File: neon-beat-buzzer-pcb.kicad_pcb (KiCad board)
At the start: 2 copper layers, 117.5 x 54.5 mm, 57 parts, among them J1 BATT_CON, J2 SWITCH_CON, J3 BUTTON_CON, J4 USB_C_Receptacle_USB2.0_16P, U1 ESP32-C3-MINI-1, U2 BQ24074RGT, U3 TPS22929D, U4 MCP1700x-330xxTT, U5 TPS610997DRV, U6 USBLC6-2SC6

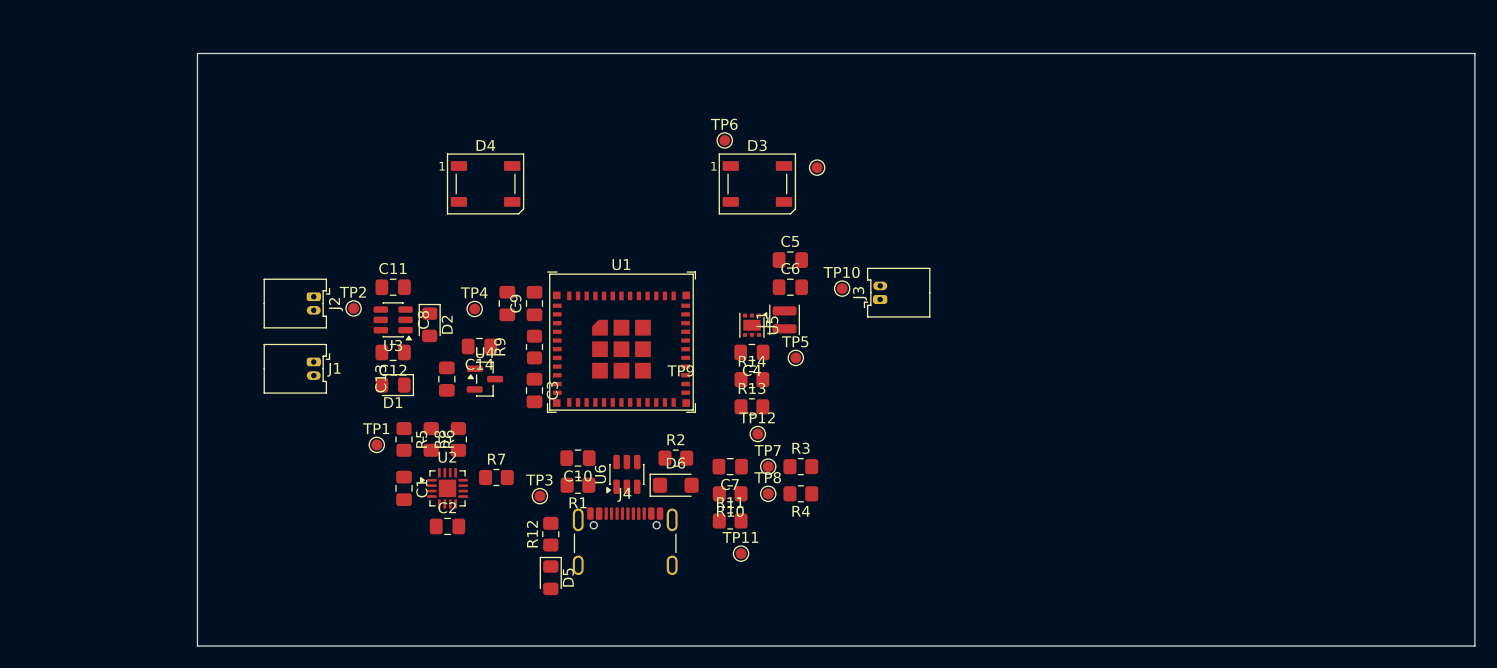
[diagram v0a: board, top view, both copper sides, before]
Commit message: pcb: add layout from Freecad
Signed-off-by: Alexis Lothoré <alexis.lothore@gmail.com>
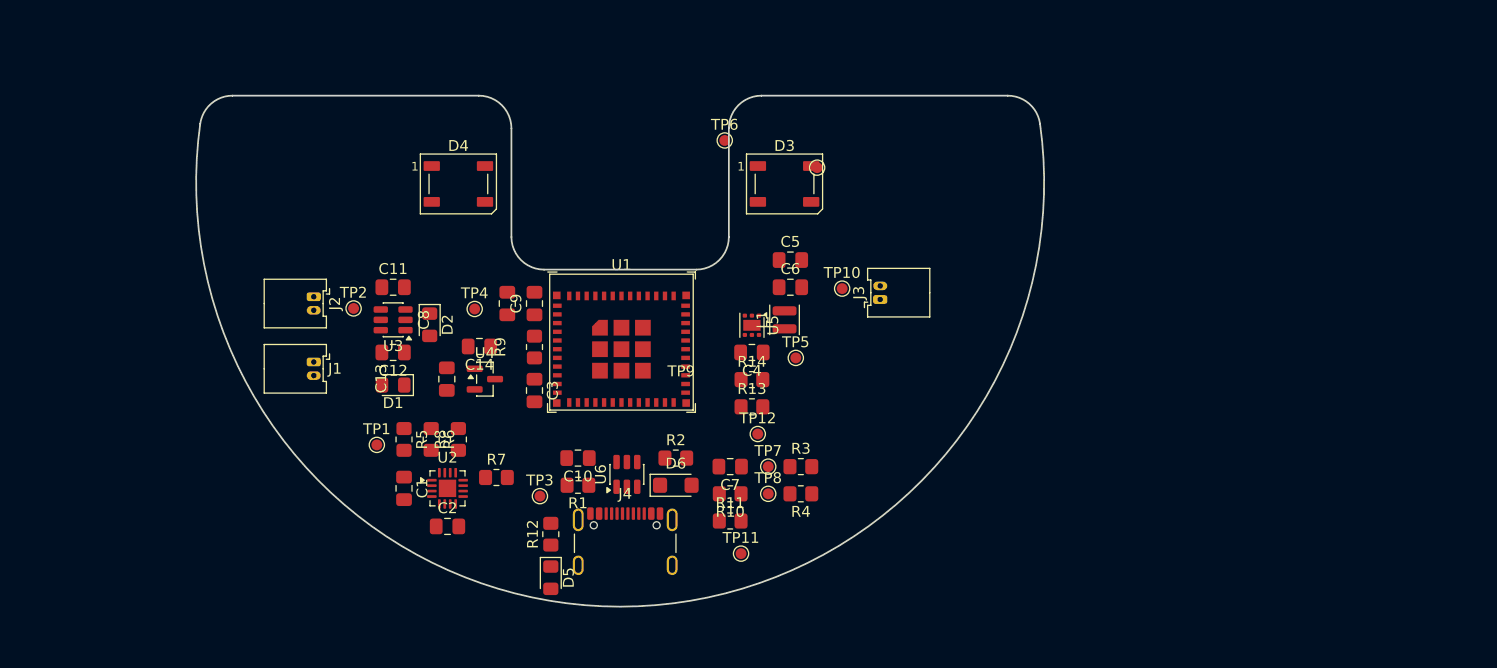
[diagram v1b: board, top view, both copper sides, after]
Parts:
- moved D3 2.50 mm to (165.0, 100.0)
- moved D4 2.50 mm to (135.0, 100.0)
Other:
- board size 117.5 x 54.5 mm -> 78 x 47 mm
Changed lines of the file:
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@@
 	(footprint "LED_SMD:LED_WS2812B_PLCC4_5.0x5.0mm_P3.2mm"
 		(layer "F.Cu")
-		(at 137.5 100)
+		(at 135 100)
 		(descr "5.0mm x 5.0mm Addressable RGB LED NeoPixel, https://cdn-shop.adafruit.com/datasheets/WS2812B.pdf")
 		(tags "LED RGB NeoPixel PLCC-4 5050")
@@
 	(footprint "LED_SMD:LED_WS2812B_PLCC4_5.0x5.0mm_P3.2mm"
 		(layer "F.Cu")
-		(at 162.5 100)
+		(at 165 100)
 		(descr "5.0mm x 5.0mm Addressable RGB LED NeoPixel, https://cdn-shop.adafruit.com/datasheets/WS2812B.pdf")
 		(tags "LED RGB NeoPixel PLCC-4 5050")
@@
 		)
 	)
-	(gr_rect
-		(start 111 88)
-		(end 228.5 142.5)
+	(gr_arc
+		(start 111.256669 94.462013)
+		(mid 112.259091 92.614834)
+		(end 114.227593 91.87868)
 		(stroke
-			(width 0.05)
-			(type default)
+			(width 0.16)
+			(type solid)
+		)
+		(layer "Edge.Cuts")
+	)
+	(gr_line
+		(start 114.227593 91.87868)
+		(end 136.87868 91.87868)
+		(stroke
+			(width 0.16)
+			(type solid)
+		)
+		(layer "Edge.Cuts")
+	)
+	(gr_arc
+		(start 136.87868 91.87868)
+		(mid 139 92.75736)
+		(end 139.87868 94.87868)
+		(stroke
+			(width 0.16)
+			(type solid)
+		)
+		(layer "Edge.Cuts")
+	)
+	(gr_line
+		(start 139.87868 94.87868)
+		(end 139.87868 104.87868)
+		(stroke
+			(width 0.16)
+			(type solid)
+		)
+		(layer "Edge.Cuts")
+	)
+	(gr_arc
+		(start 142.87868 107.87868)
+		(mid 140.75736 107)
+		(end 139.87868 104.87868)
+		(stroke
+			(width 0.16)
+			(type solid)
+		)
+		(layer "Edge.Cuts")
+	)
+	(gr_line
+		(start 142.87868 107.87868)
+		(end 156.87868 107.87868)
+		(stroke
+			(width 0.16)
+			(type solid)
+		)
+		(layer "Edge.Cuts")
+	)
+	(gr_arc
+		(start 159.87868 94.87868)
+		(mid 160.75736 92.75736)
+		(end 162.87868 91.87868)
+		(stroke
+			(width 0.16)
+			(type solid)
+		)
+		(layer "Edge.Cuts")
+	)
+	(gr_arc
+		(start 159.87868 104.87868)
+		(mid 159 107)
+		(end 156.87868 107.87868)
+		(stroke
+			(width 0.16)
+			(type solid)
+		)
+		(layer "Edge.Cuts")
+	)
+	(gr_line
+		(start 159.87868 104.87868)
+		(end 159.87868 94.87868)
+		(stroke
+			(width 0.16)
+			(type solid)
+		)
+		(layer "Edge.Cuts")
+	)
+	(gr_line
+		(start 162.87868 91.87868)
+		(end 185.529767 91.87868)
+		(stroke
+			(width 0.16)
+			(type solid)
+		)
+		(layer "Edge.Cuts")
+	)
+	(gr_arc
+		(start 185.529767 91.87868)
+		(mid 187.498276 92.614829)
+		(end 188.500691 94.462013)
+		(stroke
+			(width 0.16)
+			(type solid)
+		)
+		(layer "Edge.Cuts")
+	)
+	(gr_arc
+		(start 188.500691 94.462013)
+		(mid 149.87868 138.87868)
+		(end 111.256669 94.462013)
+		(stroke
+			(width 0.16)
+			(type solid)
 		)
-		(fill no)
 		(layer "Edge.Cuts")
 	)

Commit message: project: partial routing
Signed-off-by: Alexis Lothoré <alexis.lothore@gmail.com>
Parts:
- added C15: 0.1uF, Capacitor_SMD:C_0805_2012Metric_Pad1.18x1.45mm_HandSolder, F.Cu at (147.0, 89.5)
- added C16: 0.1uF, Capacitor_SMD:C_0805_2012Metric_Pad1.18x1.45mm_HandSolder, F.Cu at (118.0, 89.5)
- added C17: 0.1uF, Capacitor_SMD:C_0805_2012Metric_Pad1.18x1.45mm_HandSolder, F.Cu at (155.0, 115.5)
- added R16: 10k, Resistor_SMD:R_0805_2012Metric_Pad1.20x1.40mm_HandSolder, F.Cu at (164.7, 110.0)
- added U7: XC6210B332MR, Package_TO_SOT_SMD:SOT-23-5, F.Cu at (122.8, 111.8)
- U4: value MCP1700x-330xxTT -> 74AHCT1G125; footprint Package_TO_SOT_SMD:SOT-23 -> Package_TO_SOT_SMD:SOT-23-5
- moved TP5 45.5 mm to (121.5, 106.8)
- moved R4 34.1 mm to (132.5, 125.5), turned to 90 degrees
- moved TP8 33.2 mm to (130.5, 124.5)
- moved R3 32.0 mm to (134.5, 125.5), turned to 90 degrees
- moved TP10 27.5 mm to (143.5, 115.8)
- moved TP7 27.0 mm to (136.5, 124.5)
- moved TP12 26.3 mm to (136.2, 122.2)
- moved R13 23.5 mm to (138.5, 119.8), turned to 180 degrees
- moved J3 23.4 mm to (150.8, 114.5), turned to -90 degrees
- moved R1 22.5 mm to (123.5, 128.5), turned to 90 degrees
- moved U4 20.8 mm to (148.0, 100.0)
- moved R14 20.7 mm to (143.0, 109.8), turned to -90 degrees
- moved TP4 19.5 mm to (117.2, 114.8)
- moved C11 18.5 mm to (110.8, 112.8), turned to 90 degrees
- moved D6 18.0 mm to (137.0, 129.0), turned to 90 degrees
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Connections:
- C4 pad 1: /v_3v3 -> /v_sys
- D3 pad 4: /led -> Net-(D3-DIN)
- L1 pad 1: /v_3v3 -> /v_sys
- R13 pad 2: /v_3v3 -> Net-(U5-EN)
- R14 pad 2: /v_3v3 -> /v_sys
- U4 pad 2: /v_3v3 -> /led
- U4 pad 3: /v_ldo -> GND
- U5 pad 6: /v_3v3 -> /v_sys
- U6 pad 1: Net-(J4-D--PadA7) -> Net-(R4-Pad1)
- U6 pad 3: Net-(J4-D+-PadA6) -> Net-(R3-Pad1)
- U6 pad 4: Net-(R3-Pad1) -> Net-(J4-D+-PadA6)
- U6 pad 6: Net-(R4-Pad1) -> Net-(J4-D--PadA7)
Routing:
- net GND: track 0.00 -> 64.0 mm
- net /v_usb: track 0.00 -> 25.6 mm
- net /v_sys: track 0.00 -> 17.8 mm
- net /v_3v3: track 0.00 -> 15.5 mm
- net Net-(J4-CC1): track 0.00 -> 13.5 mm
- net /v_batt_p: track 0.00 -> 12.5 mm
- net /v_ldo: track 0.00 -> 11.9 mm
- net Net-(J4-CC2): track 0.00 -> 10.4 mm
- net Net-(R3-Pad1): track 0.00 -> 9.20 mm
- net Net-(J4-D--PadA7): track 0.00 -> 6.74 mm
- net /switch: track 0.00 -> 6.62 mm
- net Net-(D1-K): track 0.00 -> 6.47 mm
- net Net-(J4-D+-PadA6): track 0.00 -> 4.92 mm
- net Net-(U1-EN/CHIP_PU): track 0.00 -> 4.13 mm
- net /chg: track 0.00 -> 2.78 mm
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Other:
- board size 78 x 47 mm -> 78 x 55.1 mm

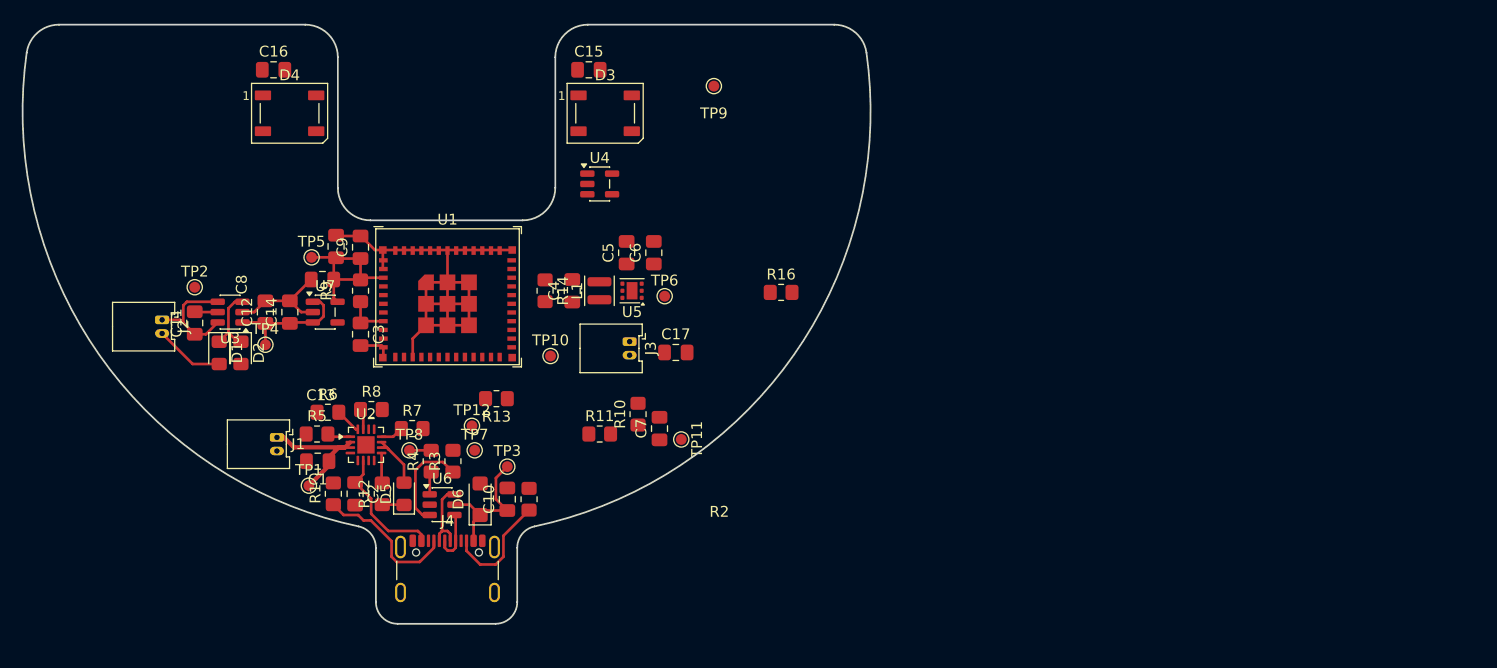
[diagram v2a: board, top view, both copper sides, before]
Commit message: project: add routed board
- Board is now fully routed (and needs some review)
- Tooling holes are added
- Needs to complete BOM

Signed-off-by: Alexis Lothoré <alexis.lothore@gmail.com>
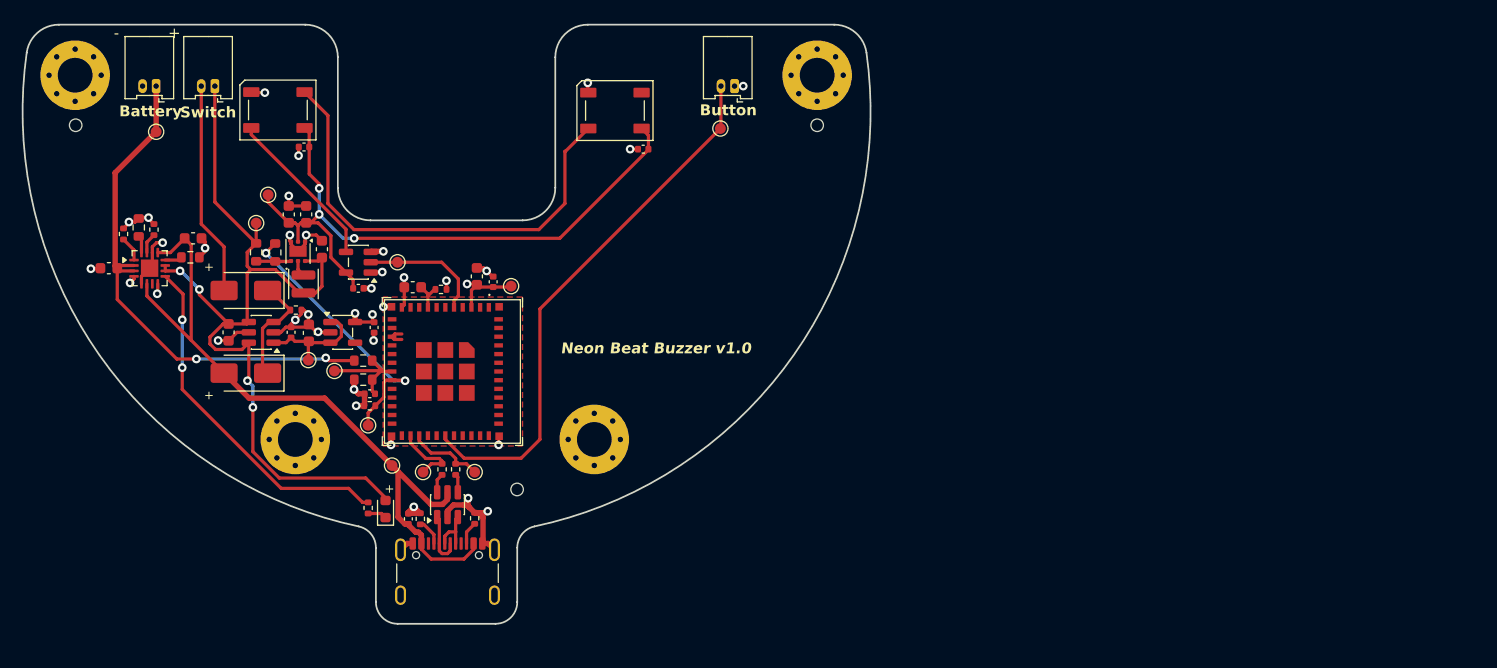
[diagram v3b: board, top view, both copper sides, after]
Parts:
- removed D1, D2: D, Diode_SMD:D_0805_2012Metric_Pad1.15x1.40mm_HandSolder
- removed D6: SMF5V0A, Diode_SMD:D_SMF
- added D7: D_Schottky, Diode_SMD:D_SMA, F.Cu at (115.5, 109.8)
- added D8: D_Schottky, Diode_SMD:D_SMA, F.Cu at (115.5, 117.4)
- added H1: ~, MountingHole:MountingHole_3.2mm_M3_Pad_Via, F.Cu at (99.8, 90.0)
- added H2: ~, MountingHole:MountingHole_3.2mm_M3_Pad_Via, F.Cu at (168.0, 90.0)
- added H3: ~, MountingHole:MountingHole_3.2mm_M3_Pad_Via, F.Cu at (147.5, 123.5)
- added H4: ~, MountingHole:MountingHole_3.2mm_M3_Pad_Via, F.Cu at (120.0, 123.5)
- added R15: 10k, Resistor_SMD:R_0402_1005Metric, F.Cu at (120.0, 111.6)
- added REF**: ToolingHole_1.152mm, MountingHole:ToolingHole_1.152mm, F.Cu at (99.8, 94.6)
- added REF**: ToolingHole_1.152mm, MountingHole:ToolingHole_1.152mm, F.Cu at (140.4, 128.1)
- added REF**: ToolingHole_1.152mm, MountingHole:ToolingHole_1.152mm, F.Cu at (168.0, 94.6)
- C1, C11, C14, C2, C3, C4, C5, C6, C9: footprint Capacitor_SMD:C_0805_2012Metric_Pad1.18x1.45mm_HandSolder -> Capacitor_SMD:C_0603_1608Metric
- C10, C12, C13, C15, C16, C17, C7, C8: footprint Capacitor_SMD:C_0805_2012Metric_Pad1.18x1.45mm_HandSolder -> Capacitor_SMD:C_0402_1005Metric
- D5: footprint Diode_SMD:D_0805_2012Metric_Pad1.15x1.40mm_HandSolder -> LED_SMD:LED_0603_1608Metric
- R1, R12, R16, R2, R3, R4, R5, R9: footprint Resistor_SMD:R_0805_2012Metric_Pad1.20x1.40mm_HandSolder -> Resistor_SMD:R_0402_1005Metric
- R10: value 100k -> 68k; footprint Resistor_SMD:R_0805_2012Metric_Pad1.20x1.40mm_HandSolder -> Resistor_SMD:R_0603_1608Metric
- R11: value 240k -> 220k; footprint Resistor_SMD:R_0805_2012Metric_Pad1.20x1.40mm_HandSolder -> Resistor_SMD:R_0603_1608Metric
- R13, R14: footprint Resistor_SMD:R_0805_2012Metric_Pad1.20x1.40mm_HandSolder -> Resistor_SMD:R_0603_1608Metric
- R6: value 2.8k -> 1.8k; footprint Resistor_SMD:R_0805_2012Metric_Pad1.20x1.40mm_HandSolder -> Resistor_SMD:R_0603_1608Metric
- R7: value 3.3k -> 3k; footprint Resistor_SMD:R_0805_2012Metric_Pad1.20x1.40mm_HandSolder -> Resistor_SMD:R_0603_1608Metric
- R8: value 2k -> 1k; footprint Resistor_SMD:R_0805_2012Metric_Pad1.20x1.40mm_HandSolder -> Resistor_SMD:R_0402_1005Metric
- moved R16 39.2 mm to (126.8, 120.4), turned to 180 degrees
- moved TP6 37.6 mm to (117.5, 101.0)
- moved TP1 35.5 mm to (107.2, 95.2)
- moved C16 34.8 mm to (152.0, 96.8), turned to 180 degrees
- moved J1 34.2 mm to (107.2, 91.0), turned to 180 degrees
- moved TP9 33.3 mm to (129.4, 107.2)
- moved TP11 32.5 mm to (123.6, 117.2), turned to 0 degrees
- moved C6 32.2 mm to (121.0, 102.8)
- moved C5 31.3 mm to (119.4, 102.8)
- moved U5 30.9 mm to (120.2, 106.2), turned to -90 degrees
- moved D3 30.1 mm to (118.4, 93.2), turned to 180 degrees
- moved D4 29.9 mm to (149.4, 93.2), turned to 180 degrees
- moved C17 29.8 mm to (125.8, 109.6)
- moved C2 27.8 mm to (110.6, 105.0), turned to 0 degrees
- moved L1 27.2 mm to (120.8, 109.2), turned to -90 degrees
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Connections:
- L1 pad 1: /v_sys -> Net-(U5-SW)
- L1 pad 2: Net-(U5-SW) -> /v_sys
- U1 pad 30: unconnected-(U1-GPIO20/U0RXD-Pad30) -> /button
- U1 pad 6: /button -> unconnected-(U1-GPIO3/ADC1_CH3-Pad6)
- U6 pad 1: Net-(R4-Pad1) -> Net-(J4-D--PadA7)
- U6 pad 3: Net-(R3-Pad1) -> Net-(J4-D+-PadA6)
- U6 pad 4: Net-(J4-D+-PadA6) -> Net-(R3-Pad1)
- U6 pad 6: Net-(J4-D--PadA7) -> Net-(R4-Pad1)
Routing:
- net /v_5v: track 0.00 -> 61.9 mm, vias 0 -> 3
- net /v_sys: track 17.8 -> 79.7 mm, vias 0 -> 4
- net /button: track 0.00 -> 49.9 mm
- net Net-(D3-DOUT): track 0.00 -> 42.7 mm
- net /v_usb: track 25.6 -> 64.7 mm
- net /v_batt_p: track 12.5 -> 48.8 mm, vias 0 -> 2
- net /chg: track 2.78 -> 32.7 mm, vias 0 -> 2
- net /boost_en: track 0.00 -> 25.5 mm, vias 0 -> 2
- net Net-(D3-DIN): track 0.00 -> 15.0 mm
- net /switch: track 6.62 -> 19.7 mm
- net /led: track 0.00 -> 11.5 mm
- net Net-(J4-CC1): track 13.5 -> 2.47 mm
- net /v_batt_meas: track 0.00 -> 10.3 mm
- net Net-(J4-CC2): track 10.4 -> 2.12 mm
- net Net-(R3-Pad1): track 9.20 -> 1.69 mm
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- added copper zone on In1.Cu, net /v_3v3
- added copper zone on F.Cu, net GND
- added copper zone on In2.Cu, net GND
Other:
- copper layers 2 -> 4
- board text added: "+"
- board text added: "-"
- board text added: "Battery"
- board text added: "Button"
- board text added: "Neon Beat Buzzer v1.0"
- board text added: "Switch"

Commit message: board: fix layout
Move the boost input from v_sys to v_ldo. Update the PCB accordingly.
While at it, import JLCPCB design rules. There are still a lot of
silkscreen clearance issues to fix.

Signed-off-by: Alexis Lothoré <alexis.lothore@gmail.com>
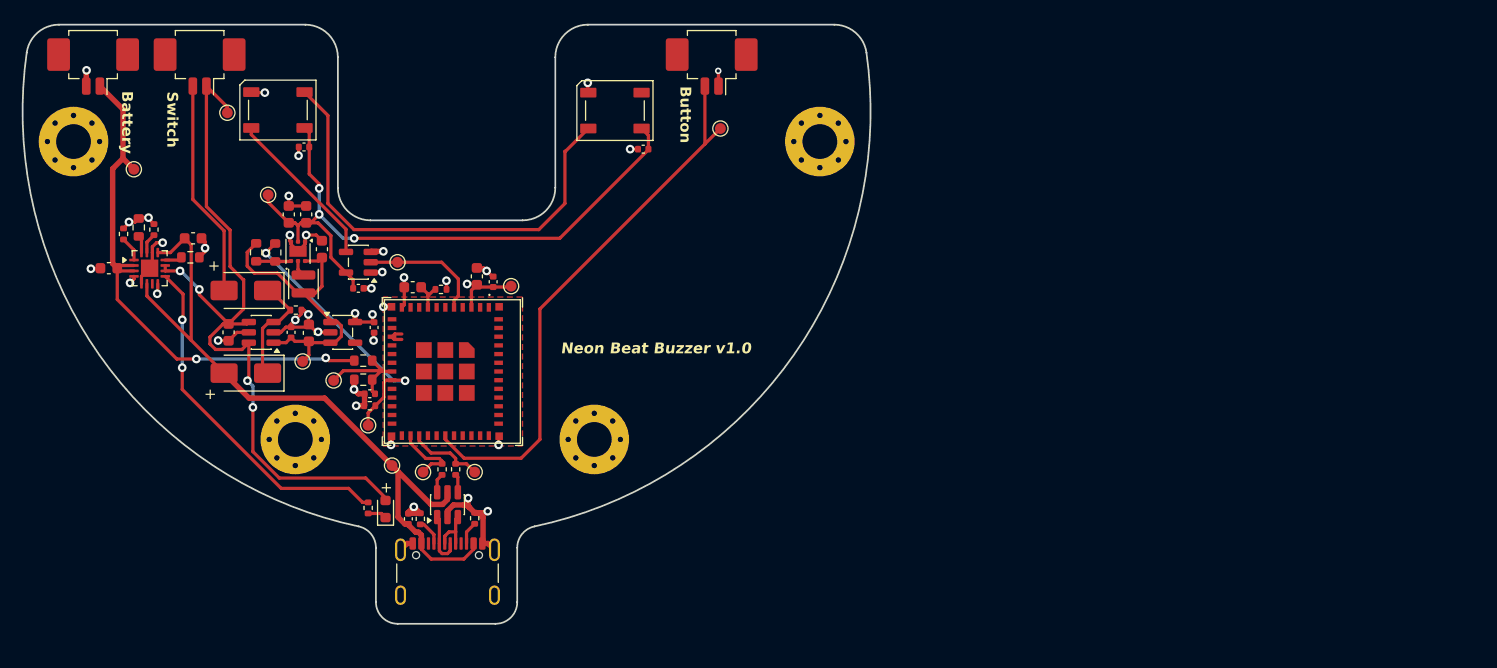
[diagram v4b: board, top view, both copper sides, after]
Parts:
- removed REF** (x3): ToolingHole_1.152mm, MountingHole:ToolingHole_1.152mm
- J1, J2, J3: footprint Connector_Molex:Molex_PicoBlade_53048-0210_1x02_P1.25mm_Horizontal -> Connector_Molex:Molex_PicoBlade_53261-0271_1x02-1MP_P1.25mm_Horizontal
- moved TP2 10.5 mm to (113.8, 93.5)
- moved J1 6.28 mm to (101.4, 88.6)
- moved H2 6.11 mm to (168.2, 96.1)
- moved H1 6.10 mm to (99.6, 96.1)
- moved TP1 4.01 mm to (105.2, 98.7)
- moved J3 3.19 mm to (158.3, 88.6)
- moved J2 2.78 mm to (111.2, 88.6)
- moved TP11 0.88 mm to (123.5, 118.1)
- moved TP4 0.54 mm to (120.7, 116.3)
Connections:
- C4 pad 1: /v_sys -> /v_ldo
- L1 pad 2: /v_sys -> /v_ldo
- R14 pad 2: /v_sys -> /v_ldo
- U5 pad 6: /v_sys -> /v_ldo
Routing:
- net /v_ldo: track 10.7 -> 29.7 mm
- net /v_sys: track 79.7 -> 68.8 mm
- net GND: track 68.8 -> 70.2 mm, vias 32 -> 33
- net /button: track 49.9 -> 51.3 mm
- net /v_batt_p: track 48.8 -> 50.0 mm
- net /v_3v3: track 11.4 -> 12.0 mm
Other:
- board text removed: "-"

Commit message: pcb: fix all DRC errors
Many components had some silkscreen clearance issue regarding JLCPCB
constraints. Fixed those by:
- editing the library footprint
  - duplicating the footprint into a user library
- removing the faulty silkscreen
- updating all components using this footprint with the override one
- re-hiding any additional silkscreen brought by the component update

Signed-off-by: Alexis Lothoré <alexis.lothore@gmail.com>
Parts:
- C10, C12, C13, C15, C16, C17, C7, C8: footprint Capacitor_SMD:C_0402_1005Metric -> components_override:C_0402_1005Metric
- R1, R12, R15, R16, R2, R3, R4, R5, R8, R9: footprint Resistor_SMD:R_0402_1005Metric -> components_override:R_0402_1005Metric
- TP1, TP10, TP11, TP12, TP2, TP3, TP4, TP5, TP6, TP7, TP8, TP9: footprint TestPoint:TestPoint_Pad_D1.0mm -> components_override:TestPoint_Pad_D1.0mm
- moved C1 0.20 mm to (102.7, 107.8)
